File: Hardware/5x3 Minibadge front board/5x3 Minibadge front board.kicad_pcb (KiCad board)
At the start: 2 copper layers, 142.2 x 91.4 mm, 24 parts, among them J1 Board to Board

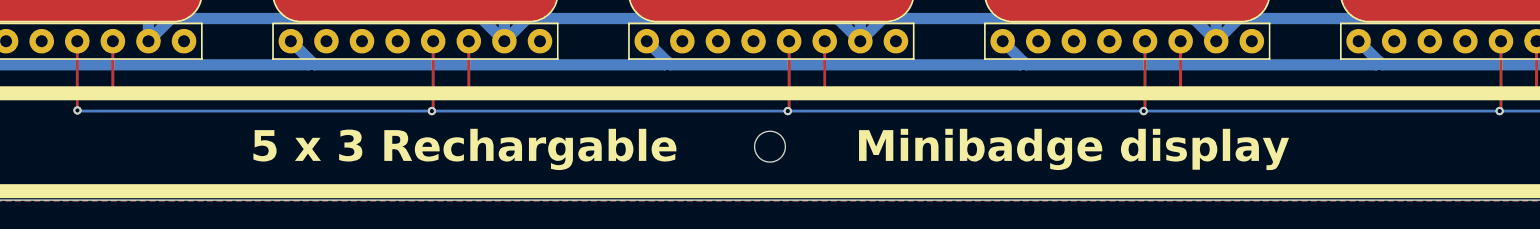
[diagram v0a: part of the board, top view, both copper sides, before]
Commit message: Silkscreen updates
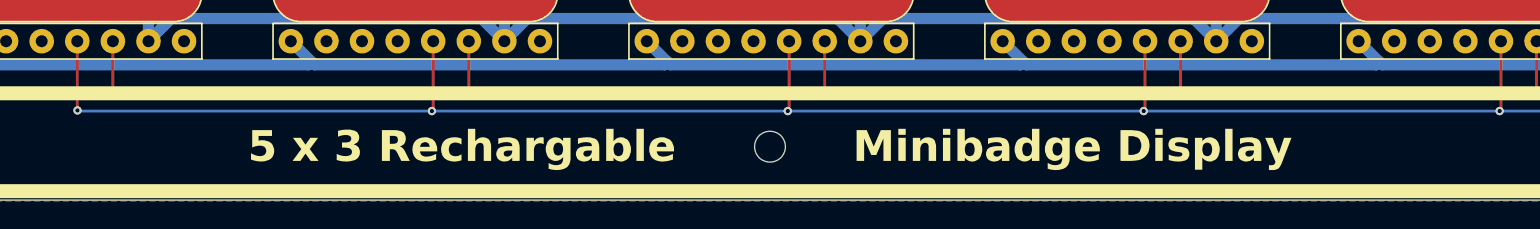
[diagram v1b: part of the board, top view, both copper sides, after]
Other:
- board text added: "5 x 3 Rechargable Minibadge Display"
- board text removed: "5 x 3 Rechargable Minibadge display"

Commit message: Fix typo
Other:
- board text added: "5 x 3 Rechargeable Minibadge Display"
- board text removed: "5 x 3 Rechargable Minibadge Display"
